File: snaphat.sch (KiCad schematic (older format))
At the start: 4 parts, among them J1 RPi_GPIO, U1 TC200, U2 RF200

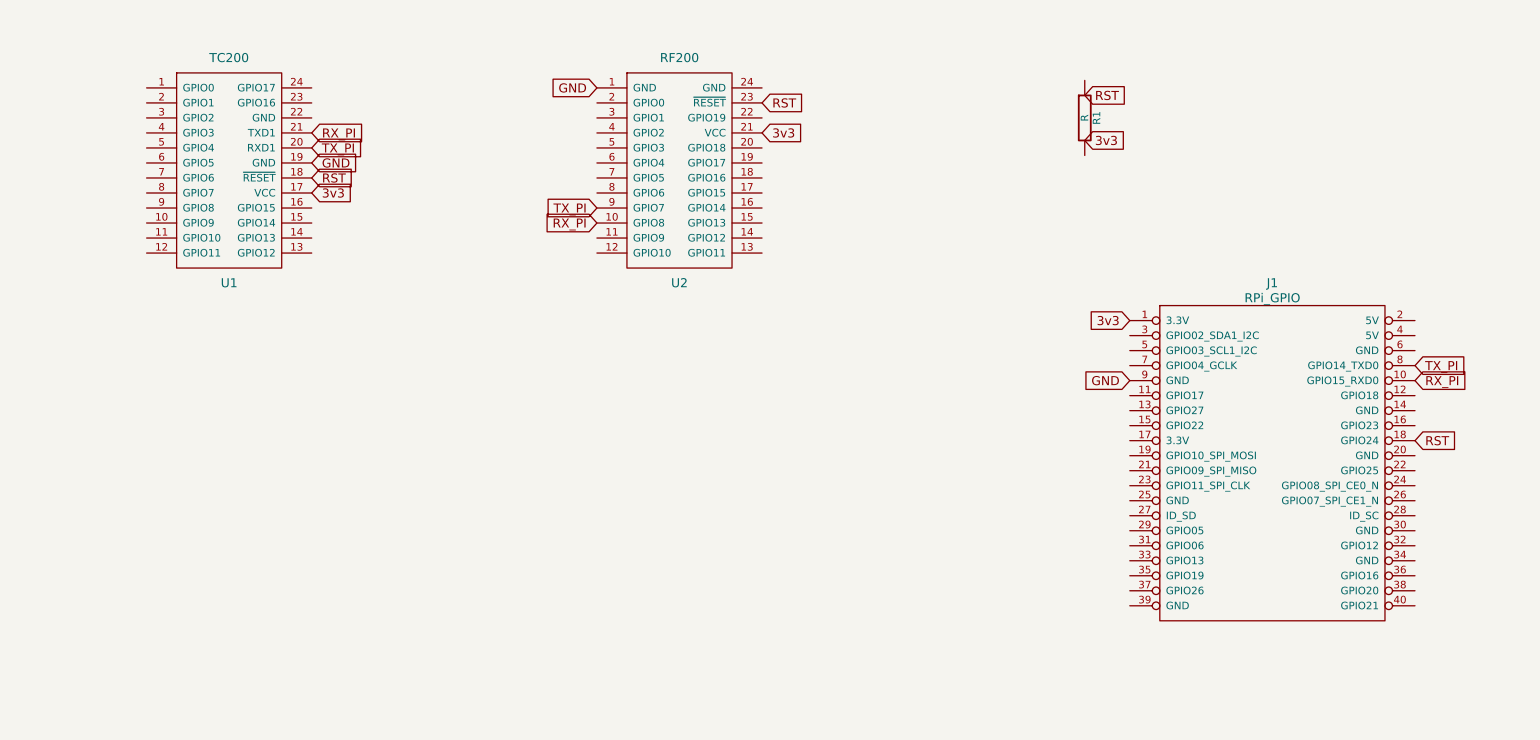
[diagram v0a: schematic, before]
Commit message: Reorganize and add i2c-serial bridge.
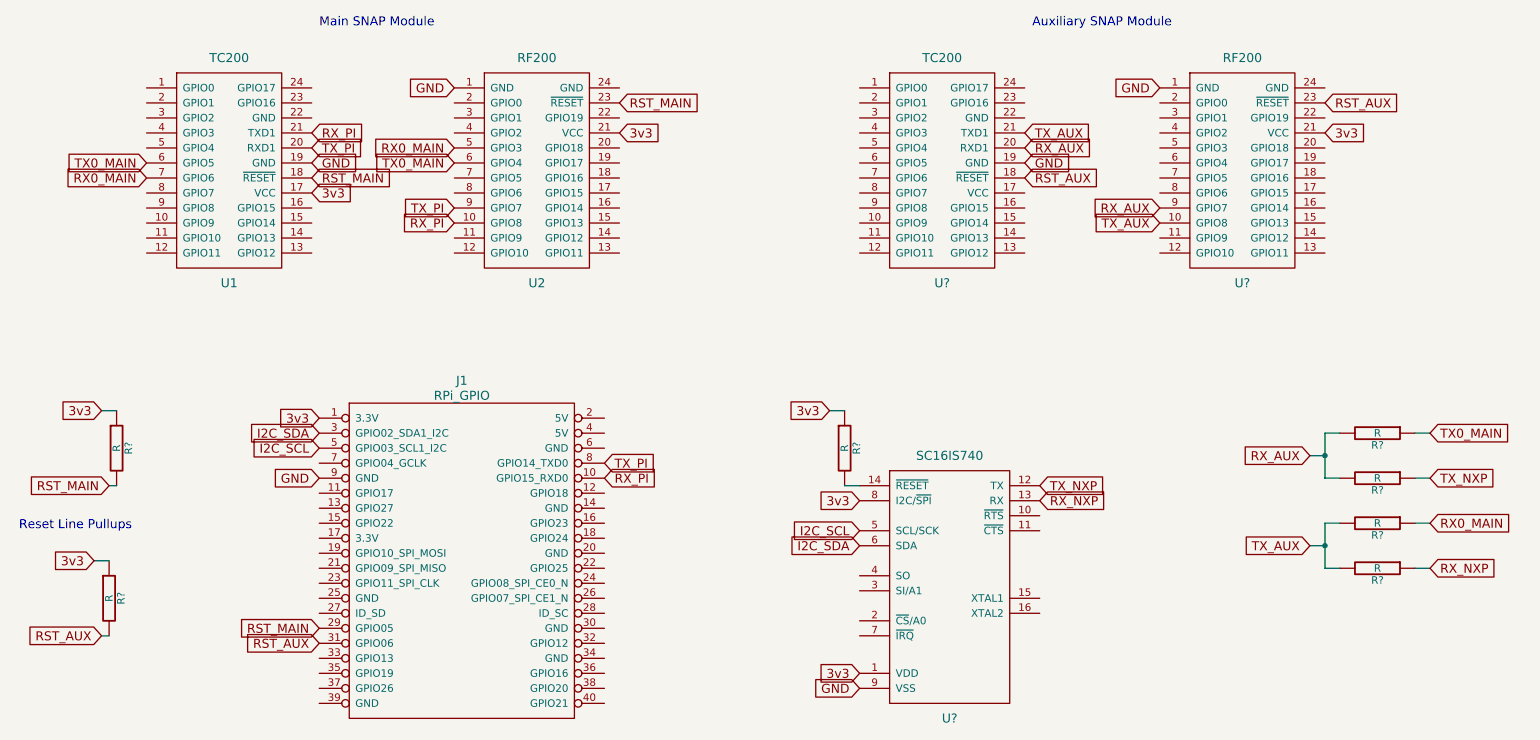
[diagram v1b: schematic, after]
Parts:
- removed R1: R, Resistors_SMD:R_0805_HandSoldering, symbol R
- added R? (x7): R, Resistors_SMD:R_0805_HandSoldering, symbol R
- added U?: SC16IS740, symbol SC16IS740
- added U?: TC200, symbol TC200
- added U?: RF200, symbol RF200
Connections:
- net 3v3: now also R?.1, R?.1, R?.1, U?.1 (VDD), U?.21 (VCC), U?.8 (I2C/~SPI)
- net GND: now also U?.1 (GND), U?.19 (GND), U?.9 (VSS)
- net RX0_MAIN: now reaches U2.5 (GPIO3)
- net RX0_MAIN: now also U1.7 (GPIO6), R?.1
- net TX0_MAIN: now reaches U2.6 (GPIO4)
- net TX0_MAIN: now also U1.6 (GPIO5), R?.1
- net RST_MAIN: now reaches J1.29 (GPIO05)
- net RST_MAIN: now also U1.18 (~RESET), U2.23 (~RESET), R?.2
- net I2C_SDA: now reaches J1.3 (GPIO02_SDA1_I2C)
- net I2C_SDA: now also U?.6 (SDA)
- net RST_AUX: now reaches J1.31 (GPIO06)
- net RST_AUX: now also R?.2, U?.18 (~RESET), U?.23 (~RESET)
- net I2C_SCL: now reaches J1.5 (GPIO03_SCL1_I2C)
- net I2C_SCL: now also U?.5 (SCL/SCK)
- removed net RST: J1.18 (GPIO24), U1.18 (~RESET), U2.23 (~RESET)
- new net: R?.2, U?.14 (~RESET)
- new net RX_AUX: R?.2, R?.2, U?.20 (RXD1), U?.9 (GPIO7)
- new net RX_NXP: R?.1, U?.13 (RX)
- new net TX_AUX: R?.2, R?.2, U?.10 (GPIO8), U?.21 (TXD1)
- new net TX_NXP: R?.1, U?.12 (TX)
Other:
- note added: "Auxiliary SNAP Module"
- note added: "Main SNAP Module"
- note added: "Reset Line Pullups"
- moved on the sheet: J1, U2
